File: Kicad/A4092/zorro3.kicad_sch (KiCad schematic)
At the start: 13 parts, among them CN1 Zorro3, U1 SN74ABT16543DGGR, U2 SN74ABT16543DGGR, U3 SN74ABT16543DGGR, U4 SN74ABT16543DGGR, U5 74LVC07APW_118, U6 SN74ABT16245ADGGR

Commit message: First version of A4770 cheetah
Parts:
- removed C5: 10pF, Capacitor_SMD:C_0603_1608Metric_Pad1.08x0.95mm_HandSolder, symbol Device:C_Small
- removed FB4, FB5: 60, Capacitor_SMD:C_0603_1608Metric_Pad1.08x0.95mm_HandSolder, symbol Device:FerriteBead_Small
- removed RN14, RN15, RN16: 1K, CAY16_102J4LF:BO_CAY16, symbol YC324-FK-071KL:YC324-FK-071KL
- added C10, C11, C12, C13, C20, C21, C22, C23, C30, C31, C32, C33, C40, C41, C42, C43, C50, C60, C61, C62, C63: 100nF, Capacitor_SMD:C_0603_1608Metric_Pad1.08x0.95mm_HandSolder, symbol Device:C_Small
- added R60, R61, R62, R63, R64, R65, R66, R67, R68, R69, R70: 1K, Resistor_SMD:R_0603_1608Metric_Pad0.98x0.95mm_HandSolder, symbol Device:R_Small
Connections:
- net GND: now also C10.2, C11.2, C12.2, C13.2, C20.2, C21.2, C22.2, C23.2, C30.2, C31.2, C32.2, C33.2, C40.2, C41.2, C42.2, C43.2, C50.2, C60.2, C61.2, C62.2, C63.2, R70.1
- net PLD_DOE: now also R70.2
- net PLD_DS0: now also R65.2
- net PLD_DS1: now also R64.2
- net PLD_DS2: now also R67.2
- net PLD_DS3: now also R66.2
- net PLD_FC0: now also R63.2
- net PLD_FC1: now also R62.2
- net PLD_FC2: now also R60.2
- net PLD_MTCR: now also R69.2
- net PLD_READ: now also R61.2
- net V3_3: now also C50.1
- net V5: now also C10.1, C11.1, C12.1, C13.1, C20.1, C21.1, C22.1, C23.1, C30.1, C31.1, C32.1, C33.1, C40.1, C41.1, C42.1, C43.1, C60.1, C61.1, C62.1, C63.1, R60.1, R61.1, R62.1, R63.1, R64.1, R65.1, R66.1, R67.1, R68.1, R69.1
- net Z_DS2: now also U6.20 (2B6)
- net Z_DS3: now also U6.19 (2B5)
- net Z_SENSEZ3: now also R68.2
- net V12: no longer names the net of CN1.10 (+12)
- no-connect marks 37 -> 36
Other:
- note removed: "Z_DS3 + Z_DS2 have FBs on original but not Z_DS1 and Z_DS0"
- moved on the sheet: CN1A, CN1B, U1, U4, U5

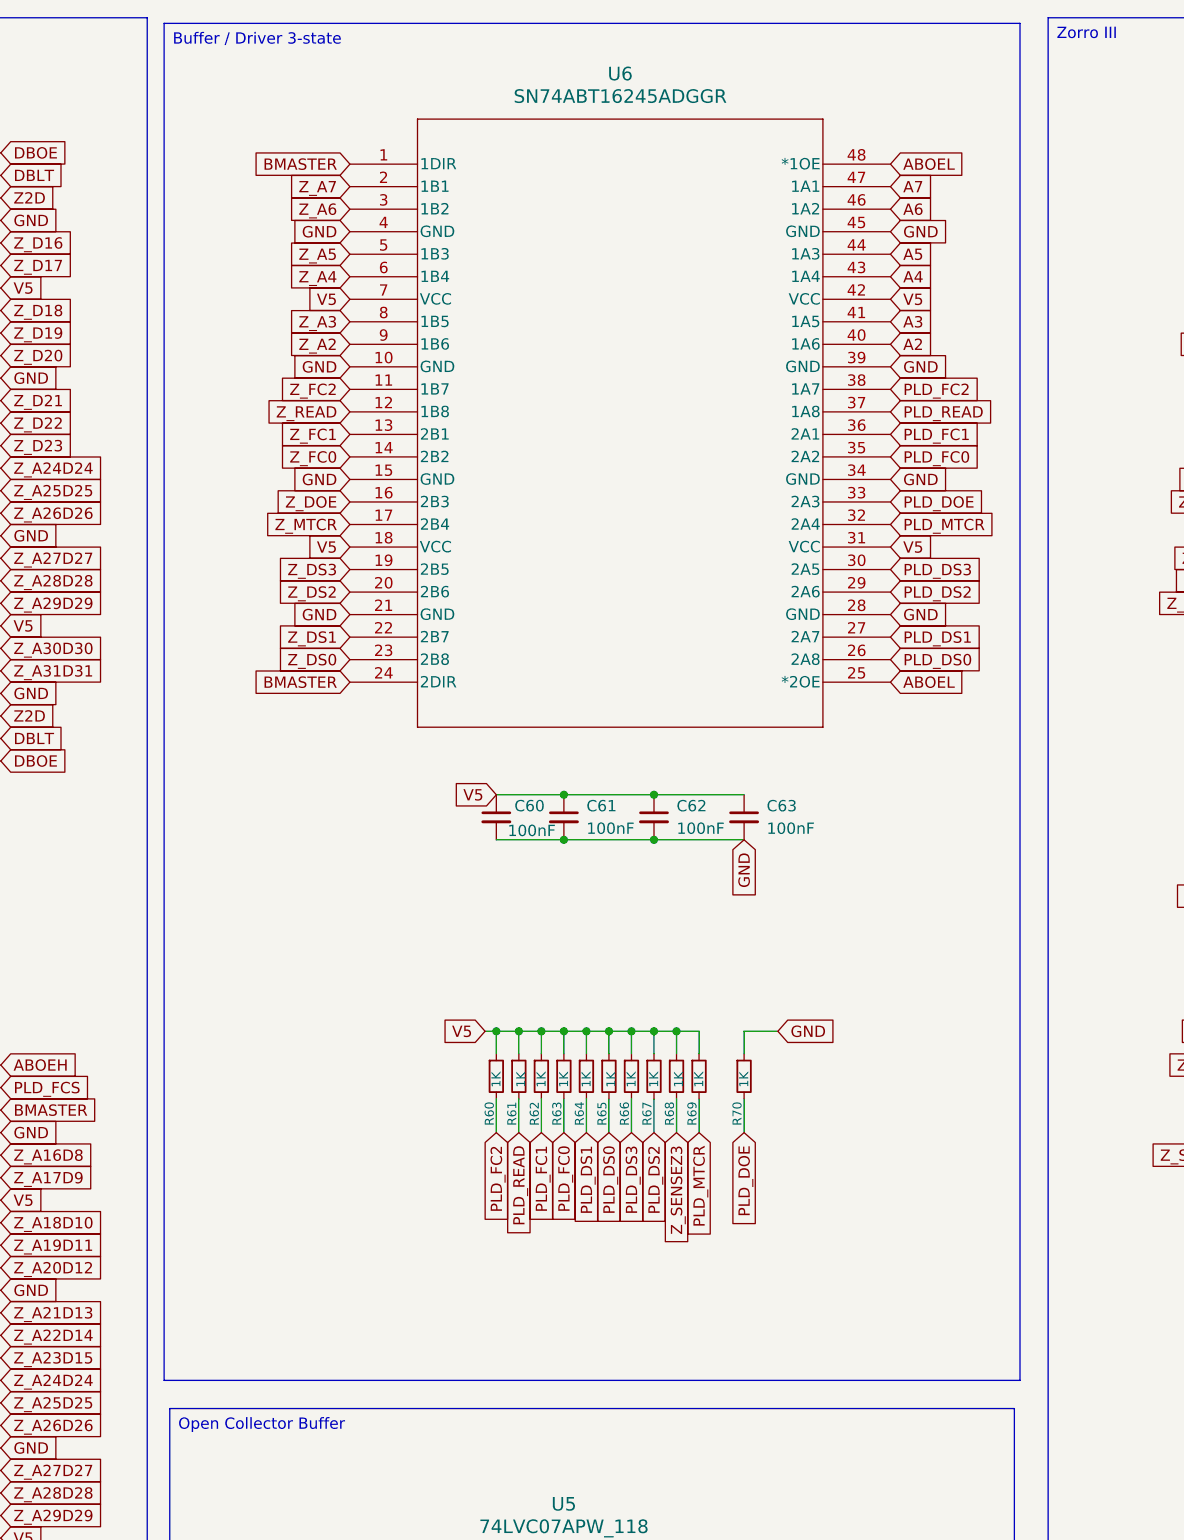
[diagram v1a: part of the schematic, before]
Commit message: U6: Switch from 74ABT16245 to 74ABT16543
This increases the number of 74ABT16543 parts used and gets rid of the
74ABT16245 all together, which overall lowers BOM cost despite the 74ABT16245
being a bit cheaper in single quantities. Given that U6 is also the only part
we know of that got killed in a Zorro accident pulling the board out of a
running machine, using a part we are more likely to have spares makes sense.
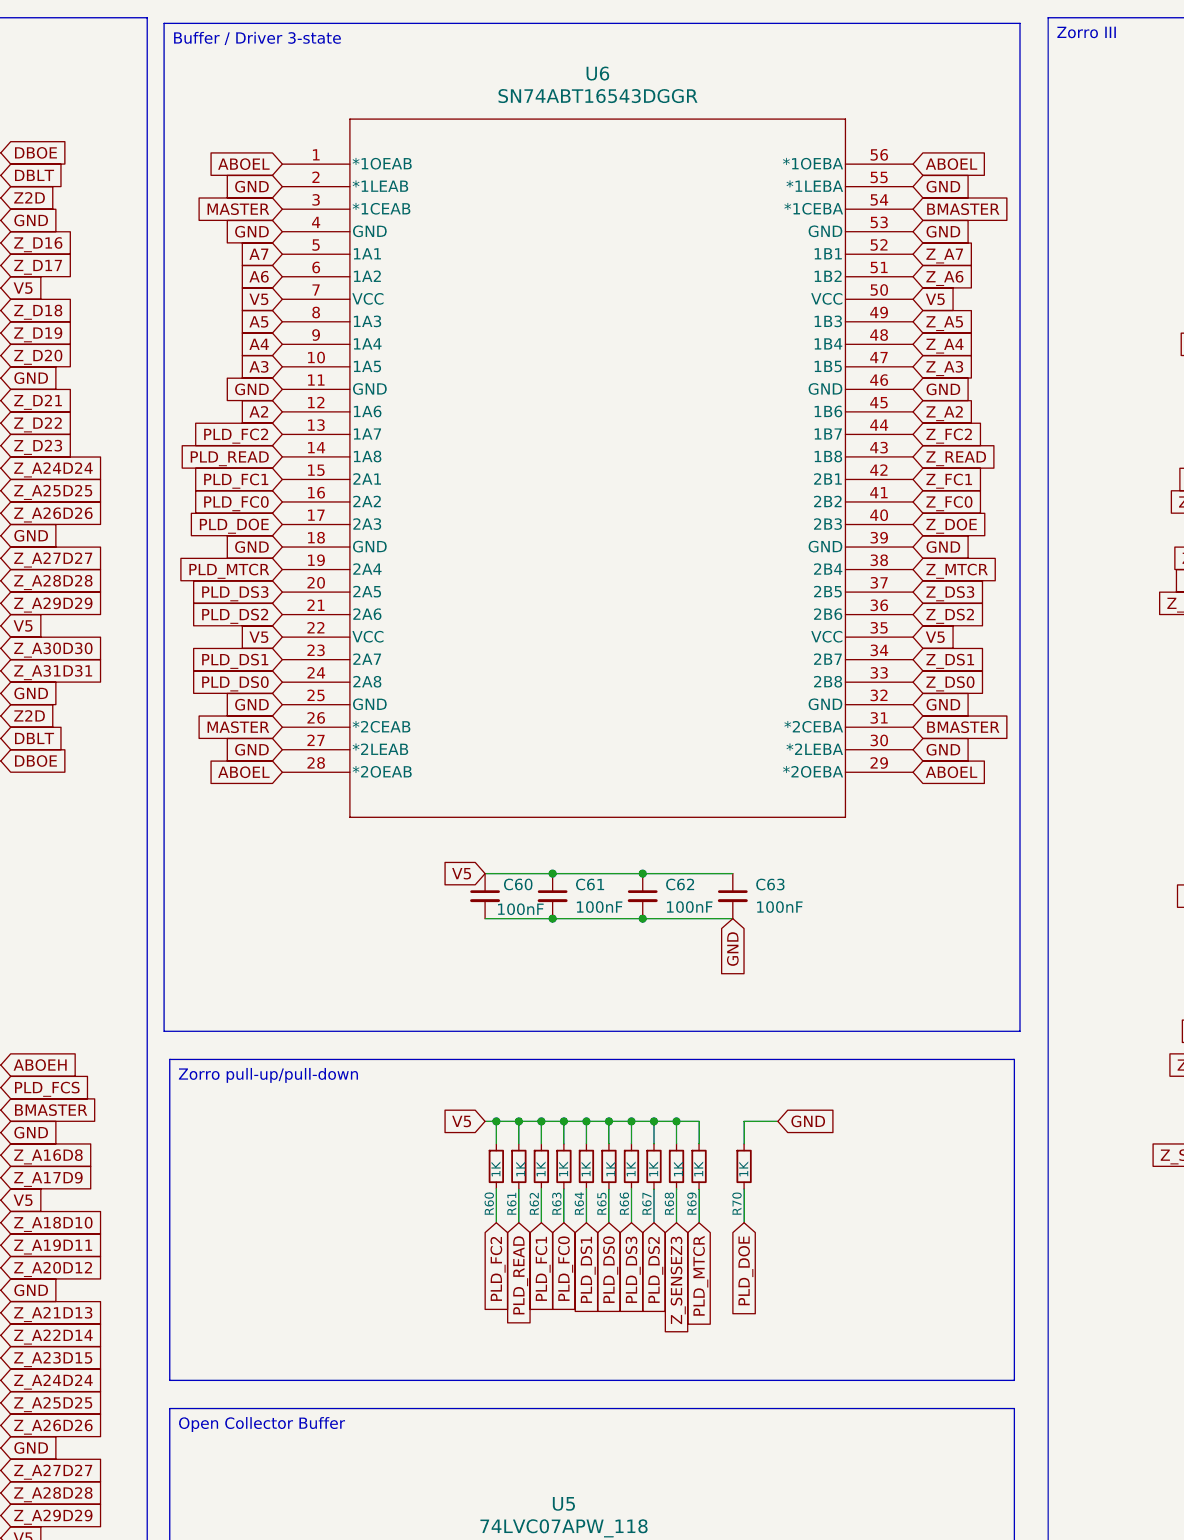
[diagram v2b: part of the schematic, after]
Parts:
- removed U6: SN74ABT16245ADGGR, SN74ABT16245ADGGR:DGG48, symbol SN74ABT16245ADGGR:SN74ABT16245ADGGR
- added U6: SN74ABT16543DGGR, DGG56, symbol SN74ABT16543DGGR:SN74ABT16543DGGR
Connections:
- net A2: now also U6.12 (1A6)
- net A3: now also U6.10 (1A5)
- net A4: now also U6.9 (1A4)
- net A5: now also U6.8 (1A3)
- net A6: now also U6.6 (1A2)
- net A7: now also U6.5 (1A1)
- net ABOEL: now also U6.1 (*1OEAB), U6.28 (*2OEAB), U6.29 (*2OEBA), U6.56 (*1OEBA)
- net BMASTER: now also U6.31 (*2CEBA), U6.54 (*1CEBA)
- net GND: now also U6.11 (GND), U6.18 (GND), U6.2 (*1LEAB), U6.25 (GND), U6.27 (*2LEAB), U6.30 (*2LEBA), U6.32 (GND), U6.39 (GND), U6.4 (GND), U6.46 (GND), U6.53 (GND), U6.55 (*1LEBA)
- net MASTER: now also U6.26 (*2CEAB), U6.3 (*1CEAB)
- net PLD_DOE: now also U6.17 (2A3)
- net PLD_DS0: now also U6.24 (2A8)
- net PLD_DS1: now also U6.23 (2A7)
- net PLD_DS2: now also U6.21 (2A6)
- net PLD_DS3: now also U6.20 (2A5)
- net PLD_FC0: now also U6.16 (2A2)
- net PLD_FC1: now also U6.15 (2A1)
- net PLD_FC2: now also U6.13 (1A7)
- net PLD_MTCR: now also U6.19 (2A4)
- net PLD_READ: now also U6.14 (1A8)
- net V5: now also U6.22 (VCC), U6.35 (VCC), U6.50 (VCC), U6.7 (VCC)
- net Z_A2: now also U6.45 (1B6)
- net Z_A3: now also U6.47 (1B5)
- net Z_A4: now also U6.48 (1B4)
- net Z_A5: now also U6.49 (1B3)
- net Z_A6: now also U6.51 (1B2)
- net Z_A7: now also U6.52 (1B1)
- net Z_DOE: now also U6.40 (2B3)
- net Z_DS0: now also U6.33 (2B8)
- net Z_DS1: now also U6.34 (2B7)
- net Z_DS2: now also U6.36 (2B6)
- net Z_DS3: now also U6.37 (2B5)
- net Z_FC0: now also U6.41 (2B2)
- net Z_FC1: now also U6.42 (2B1)
- net Z_FC2: now also U6.44 (1B7)
- net Z_MTCR: now also U6.38 (2B4)
- net Z_READ: now also U6.43 (1B8)
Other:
- moved on the sheet: C60, C61, C62, C63, R60, R61, R62, R63, R64, R65, R66, R67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

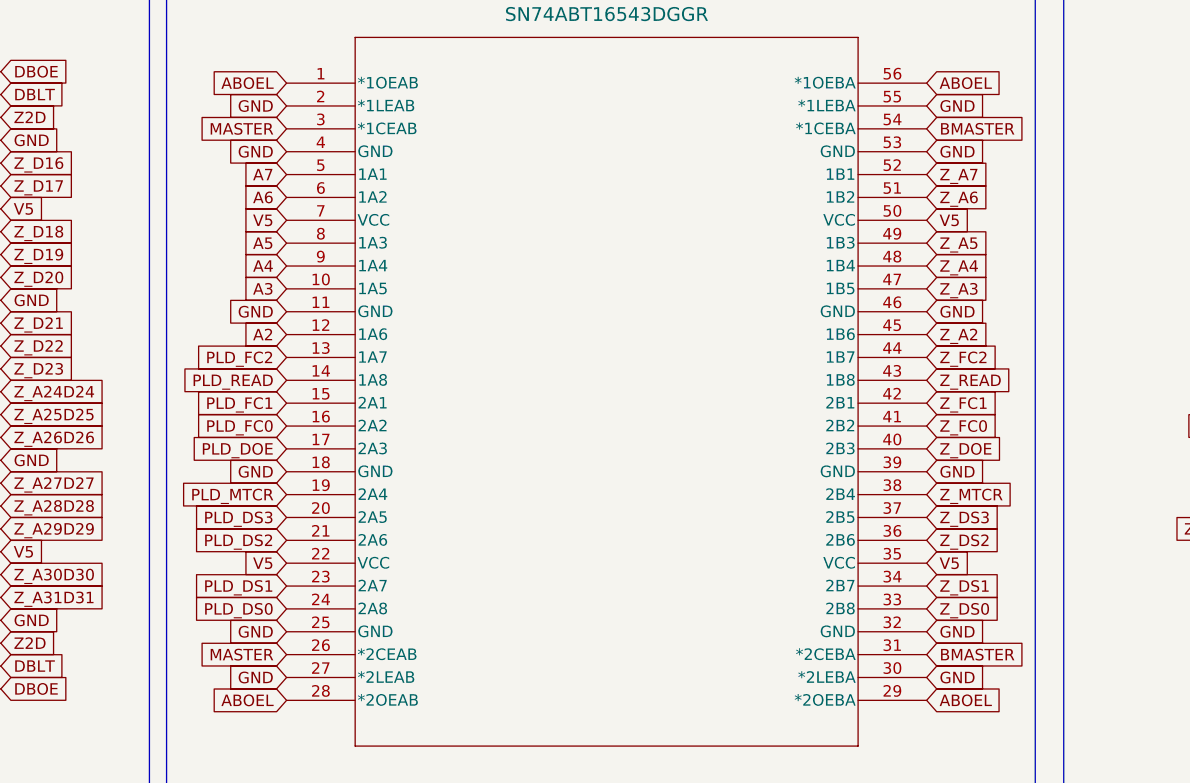
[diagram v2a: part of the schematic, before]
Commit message: Reverse pin order on U6
the pin lineup changed between 16245 and 16543. Switching the pins around
will make it easier to reroute to the new chip.
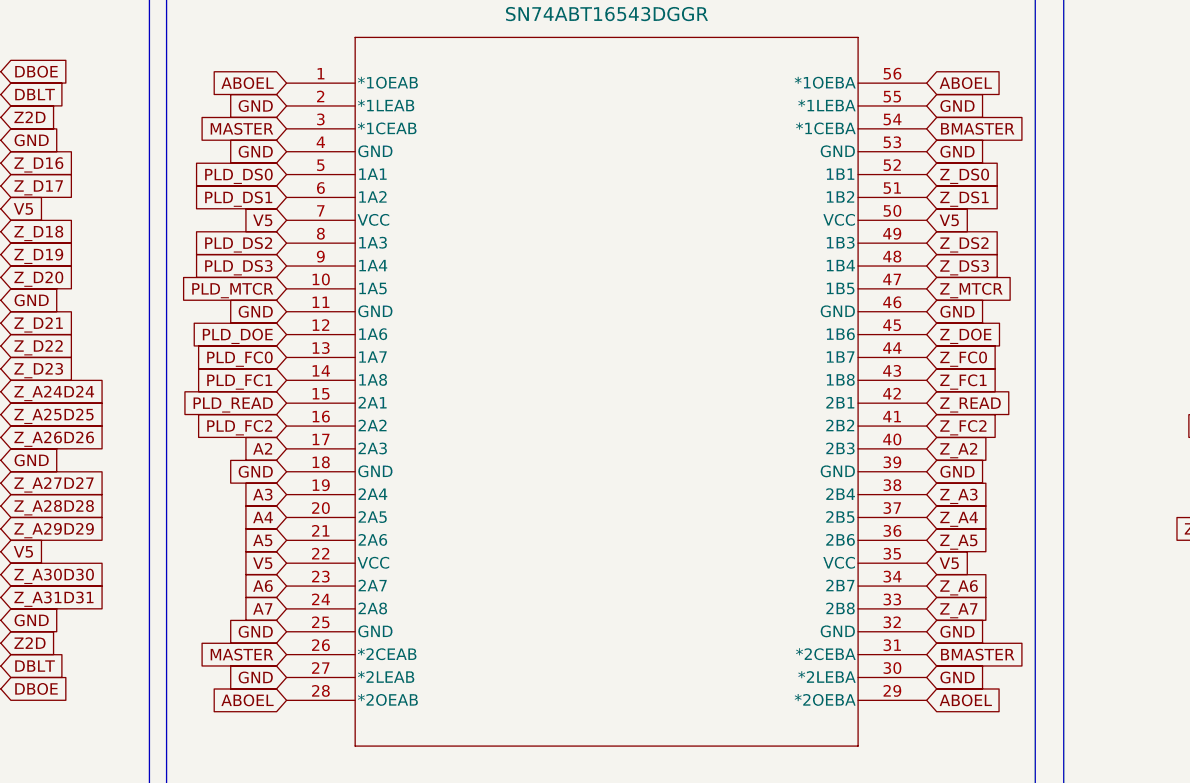
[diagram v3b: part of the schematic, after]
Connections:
- net A2: now also U6.17 (2A3); no longer U6.12 (1A6)
- net A3: now also U6.19 (2A4); no longer U6.10 (1A5)
- net A4: now also U6.20 (2A5); no longer U6.9 (1A4)
- net A5: now also U6.21 (2A6); no longer U6.8 (1A3)
- net A6: now also U6.23 (2A7); no longer U6.6 (1A2)
- net A7: now also U6.24 (2A8); no longer U6.5 (1A1)
- net PLD_DOE: now also U6.12 (1A6); no longer U6.17 (2A3)
- net PLD_DS0: now also U6.5 (1A1); no longer U6.24 (2A8)
- net PLD_DS1: now also U6.6 (1A2); no longer U6.23 (2A7)
- net PLD_DS2: now also U6.8 (1A3); no longer U6.21 (2A6)
- net PLD_DS3: now also U6.9 (1A4); no longer U6.20 (2A5)
- net PLD_FC0: now also U6.13 (1A7); no longer U6.16 (2A2)
- net PLD_FC1: now also U6.14 (1A8); no longer U6.15 (2A1)
- net PLD_FC2: now also U6.16 (2A2); no longer U6.13 (1A7)
- net PLD_MTCR: now also U6.10 (1A5); no longer U6.19 (2A4)
- net PLD_READ: now also U6.15 (2A1); no longer U6.14 (1A8)
- net Z_A2: now also U6.40 (2B3); no longer U6.45 (1B6)
- net Z_A3: now also U6.38 (2B4); no longer U6.47 (1B5)
- net Z_A4: now also U6.37 (2B5); no longer U6.48 (1B4)
- net Z_A5: now also U6.36 (2B6); no longer U6.49 (1B3)
- net Z_A6: now also U6.34 (2B7); no longer U6.51 (1B2)
- net Z_A7: now also U6.33 (2B8); no longer U6.52 (1B1)
- net Z_DOE: now also U6.45 (1B6); no longer U6.40 (2B3)
- net Z_DS0: now also U6.52 (1B1); no longer U6.33 (2B8)
- net Z_DS1: now also U6.51 (1B2); no longer U6.34 (2B7)
- net Z_DS2: now also U6.49 (1B3); no longer U6.36 (2B6)
- net Z_DS3: now also U6.48 (1B4); no longer U6.37 (2B5)
- net Z_FC0: now also U6.44 (1B7); no longer U6.41 (2B2)
- net Z_FC1: now also U6.43 (1B8); no longer U6.42 (2B1)
- net Z_FC2: now also U6.41 (2B2); no longer U6.44 (1B7)
- net Z_MTCR: now also U6.47 (1B5); no longer U6.38 (2B4)
- net Z_READ: now also U6.42 (2B1); no longer U6.43 (1B8)

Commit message: Clean up pull-up resistors
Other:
- title: A4092 -> Cheetah UW
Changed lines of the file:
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@@
 	(paper "A3")
 	(title_block
-		(title "A4092")
-		(rev "PROTO0")
+		(title "Cheetah UW")
+		(rev "PROTO1")
 		(company "amiga.technology")
 	)

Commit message: Rehaul clock circuit in schematics
and try to add most of the LCSC part numbers
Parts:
- R60, R61, R62, R63, R64, R65, R66, R67, R68, R69, R70: LCSC Part # (none) -> C21190
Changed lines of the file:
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@@
 			)
 		)
+		(property "LCSC Part #" "C21190"
+			(at 270.51 144.78 90)
+			(effects
+				(font
+					(size 1.27 1.27)
+				)
+				(hide yes)
+			)
+		)
 		(pin "2"
 		)
@@
 			)
 		)
+		(property "LCSC Part #" "C21190"
+			(at 252.73 144.78 90)
+			(effects
+				(font
+					(size 1.27 1.27)
+				)
+				(hide yes)
+			)
+		)
 		(pin "2"
 		)
@@
 			)
 		)
+		(property "LCSC Part #" "C21190"
+			(at 265.43 144.78 90)
+			(effects
+				(font
+					(size 1.27 1.27)
+				)
+				(hide yes)
+			)
+		)
 		(pin "2"
 		)
@@
 			)
 		)
+		(property "LCSC Part #" "C21190"
+			(at 273.05 144.78 90)
+			(effects
+				(font
+					(size 1.27 1.27)
+				)
+				(hide yes)
+			)
+		)
 		(pin "2"
 		)
@@
 			)
 		)
+		(property "LCSC Part #" "C21190"
+			(at 267.97 144.78 90)
+			(effects
+				(font
+					(size 1.27 1.27)
+				)
+				(hide yes)
+			)
+		)
 		(pin "2"
 		)
@@
 			)
 		)
+		(property "LCSC Part #" "C21190"
+			(at 280.67 144.78 90)
+			(effects
+				(font
+					(size 1.27 1.27)
+				)
+				(hide yes)
+			)
+		)
 		(pin "2"
 		)
@@
 			)
 		)
+		(property "LCSC Part #" "C21190"
+			(at 255.27 144.78 90)
+			(effects
+				(font
+					(size 1.27 1.27)
+				)
+				(hide yes)
+			)
+		)
 		(pin "2"
 		)
@@
 			)
 		)
+		(property "LCSC Part #" "C21190"
+			(at 257.81 144.78 90)
+			(effects
+				(font
+					(size 1.27 1.27)
+				)
+				(hide yes)
+			)
+		)
 		(pin "2"
 		)
@@
 			)
 		)
+		(property "LCSC Part #" "C21190"
+			(at 275.59 144.78 90)
+			(effects
+				(font
+					(size 1.27 1.27)
+				)
+				(hide yes)
+			)
+		)
 		(pin "2"
 		)
@@
 			)
 		)
+		(property "LCSC Part #" "C21190"
+			(at 262.89 144.78 90)
+			(effects
+				(font
+					(size 1.27 1.27)
+				)
+				(hide yes)
+			)
+		)
 		(pin "2"
 		)
@@
 			(effects
 				(font
+					(size 1.27 1.27)
+				)
+				(hide yes)
+			)
+		)
+		(property "LCSC Part #" "C21190"
+			(at 260.35 144.78 90)
+			(effects
+				(font
